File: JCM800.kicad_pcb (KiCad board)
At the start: 2 copper layers, 196 x 77.3 mm, 75 parts, among them U1 ECC83, U2 ECC83, U3 EL84

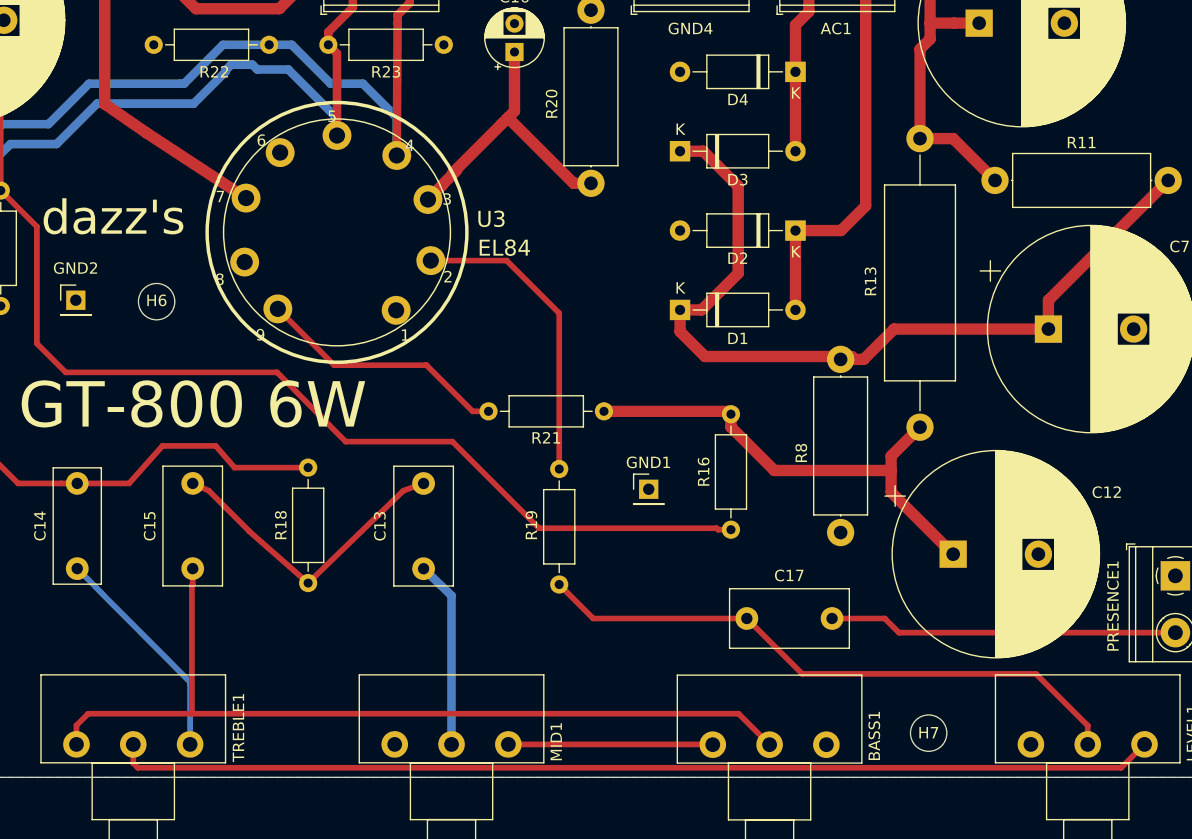
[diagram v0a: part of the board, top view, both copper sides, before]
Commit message: Added attenuation resistor
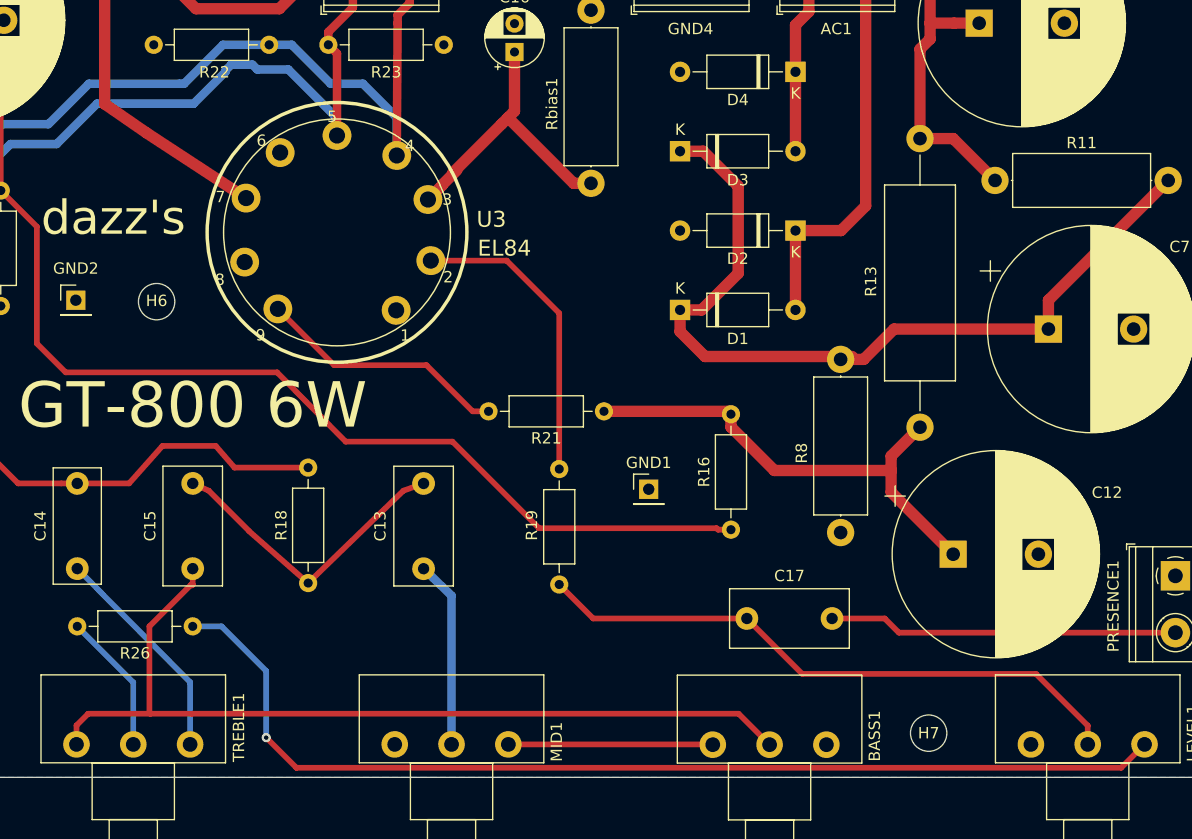
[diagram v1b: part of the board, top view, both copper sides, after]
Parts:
- added R26: ?R, Resistor_THT:R_Axial_DIN0207_L6.3mm_D2.5mm_P10.16mm_Horizontal, F.Cu at (151.1, 118.1)
- renumbered R20 to Rbias1
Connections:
- TREBLE1 pad 2: Net-(LEVEL1-Pad3) -> Net-(R26-Pad2)
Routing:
- net Net-(R26-Pad2): track 0.00 -> 12.4 mm
- net Net-(BASS1-Pad2): track 78.1 -> 79.8 mm
- net Net-(LEVEL1-Pad3): track 91.7 -> 93.2 mm, vias 0 -> 1

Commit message: Tweaks
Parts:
- C16: footprint Capacitor_THT:CP_Radial_D5.0mm_P2.50mm -> Capacitor_THT:CP_Radial_D8.0mm_P3.50mm
- moved Rbias1 0.38 mm to (186.6, 63.9)
- moved C16 0.25 mm to (179.2, 67.6)
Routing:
- net /B1: track 107.1 -> 105.9 mm

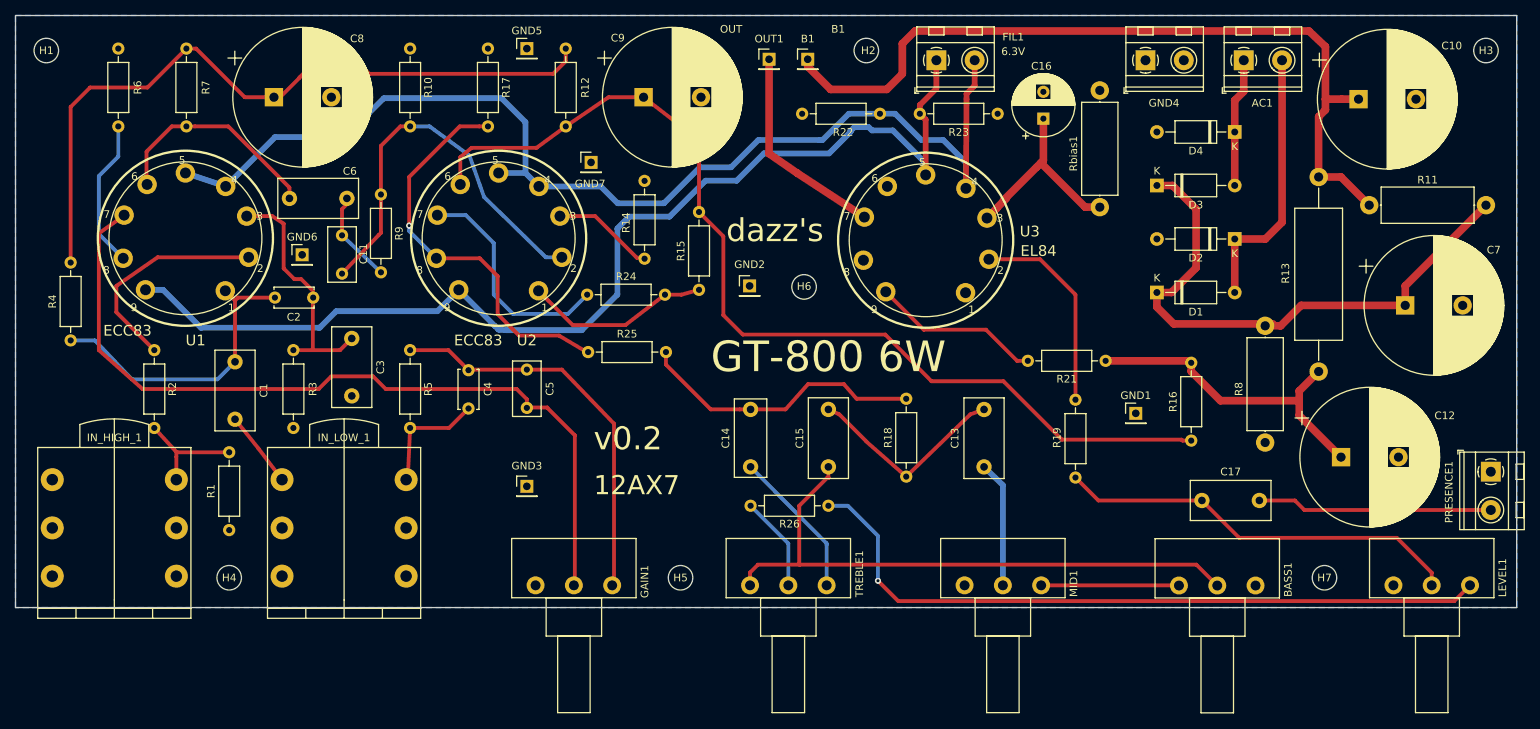
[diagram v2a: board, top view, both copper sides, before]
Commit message: Gain trace shielded
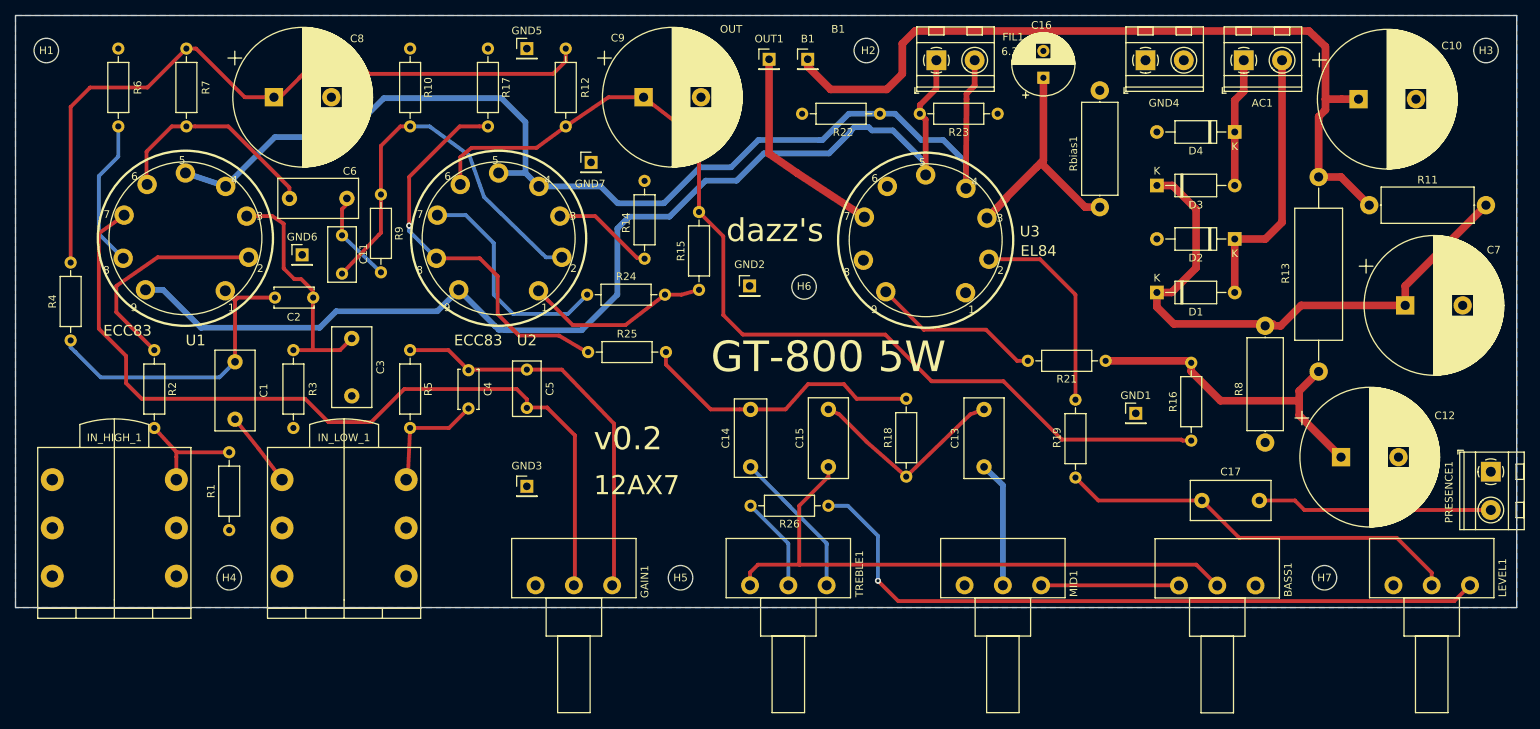
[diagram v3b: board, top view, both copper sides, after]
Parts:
- moved C16 5.33 mm to (179.2, 62.2)
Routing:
- net /EL84-CATHODE: track 26.5 -> 31.9 mm
- net Net-(C5-Pad2): track 107.6 -> 110.4 mm
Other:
- board text added: "GT-800 5W"
- board text removed: "GT-800 6W"
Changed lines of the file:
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@@
     (thickness 1.6)
     (drawings 11)
-    (tracks 325)
+    (tracks 329)
     (zones 0)
     (modules 76)
@@
     (add_net "Net-(BASS1-Pad1)")
     (add_net "Net-(BASS1-Pad2)")
+    (add_net "Net-(C1-Pad1)")
     (add_net "Net-(C1-Pad2)")
     (add_net "Net-(C11-Pad1)")
@@
     (uvia_dia 0.3)
     (uvia_drill 0.1)
-    (add_net "Net-(C1-Pad1)")
     (add_net "Net-(C13-Pad1)")
     (add_net "Net-(C14-Pad2)")
@@
   )
   (module Capacitor_THT:CP_Radial_D8.0mm_P3.50mm (layer F.Cu)
-    (at 179.197 67.564 90)
+    (at 179.197 62.23 90)
     (descr "CP, Radial series, Radial, pin pitch=3.50mm, , diameter=8mm, Electrolytic Capacitor")
     (tags "CP Radial series Radial pin pitch 3.50mm  diameter 8mm Electrolytic Capacitor")
@@
     (effects (font (size 3 3) (thickness 0.3)))
   )
-  (gr_text "GT-800 6W" (at 151.13 98.679) (layer F.SilkS)
+  (gr_text "GT-800 5W" (at 151.13 98.679) (layer F.SilkS)
     (effects (font (size 4 4) (thickness 0.5)))
   )
@@
   (segment (start 74.040998 90.932) (end 73.659999 91.312999) (width 0.5) (layer F.Cu) (net 4))
   (segment (start 78.867 90.932) (end 74.040998 90.932) (width 0.5) (layer F.Cu) (net 4) (status 10))
-  (segment (start 71.374 101.6) (end 73.66 99.314) (width 0.5) (layer B.Cu) (net 4) (status 20))
-  (segment (start 55.36037 96.52) (end 52.197 96.52) (width 0.5) (layer B.Cu) (net 4) (status 20))
-  (segment (start 60.198 101.6) (end 71.374 101.6) (width 0.5) (layer B.Cu) (net 4))
-  (segment (start 55.36037 96.52) (end 60.198 101.6) (width 0.5) (layer B.Cu) (net 4))
+  (segment (start 52.832 98.044) (end 52.180868 97.424058) (width 0.5) (layer B.Cu) (net 4))
+  (segment (start 56.134 101.346) (end 52.832 98.044) (width 0.5) (layer B.Cu) (net 4))
+  (segment (start 73.66 99.314) (end 71.628 101.346) (width 0.5) (layer B.Cu) (net 4))
+  (segment (start 71.628 101.346) (end 56.134 101.346) (width 0.5) (layer B.Cu) (net 4))
+  (segment (start 52.180868 96.536132) (end 52.197 96.52) (width 0.5) (layer B.Cu) (net 4))
+  (segment (start 52.180868 97.424058) (end 52.180868 96.536132) (width 0.5) (layer B.Cu) (net 4))
   (segment (start 83.82 97.79) (end 83.82 90.043) (width 0.5) (layer F.Cu) (net 5))
   (segment (start 83.82 90.043) (end 82.296 88.519) (width 0.5) (layer F.Cu) (net 5))
@@
   (segment (start 114.427 105.316) (end 118.03 108.919) (width 0.5) (layer F.Cu) (net 9))
   (segment (start 114.427 105.283) (end 114.427 105.316) (width 0.5) (layer F.Cu) (net 9))
-  (segment (start 111.76 104.19863) (end 111.76 105.33) (width 0.5) (layer F.Cu) (net 9) (status 20))
-  (segment (start 110.43137 102.87) (end 111.76 104.19863) (width 0.5) (layer F.Cu) (net 9))
-  (segment (start 93.345 102.87) (end 110.43137 102.87) (width 0.5) (layer F.Cu) (net 9))
-  (segment (start 91.694 101.219) (end 93.345 102.87) (width 0.5) (layer F.Cu) (net 9))
-  (segment (start 55.88 82.55) (end 55.88 97.79) (width 0.5) (layer F.Cu) (net 9))
-  (segment (start 59.25 80.166) (end 55.88 82.55) (width 0.5) (layer F.Cu) (net 9) (status 10))
-  (segment (start 55.88 97.79) (end 61.595 102.87) (width 0.5) (layer F.Cu) (net 9))
-  (segment (start 61.595 102.87) (end 84.582 102.87) (width 0.5) (layer F.Cu) (net 9))
-  (segment (start 84.582 102.87) (end 86.233 101.219) (width 0.5) (layer F.Cu) (net 9))
-  (segment (start 86.233 101.219) (end 91.694 101.219) (width 0.5) (layer F.Cu) (net 9))
+  (segment (start 55.88 82.55) (end 59.25 80.166) (width 0.5) (layer F.Cu) (net 9))
+  (segment (start 55.88 94.996) (end 55.88 82.55) (width 0.5) (layer F.Cu) (net 9))
+  (segment (start 59.436 98.552) (end 55.88 94.996) (width 0.5) (layer F.Cu) (net 9))
+  (segment (start 59.436 102.108) (end 59.436 98.552) (width 0.5) (layer F.Cu) (net 9))
+  (segment (start 61.468 104.14) (end 59.436 102.108) (width 0.5) (layer F.Cu) (net 9))
+  (segment (start 82.804 104.14) (end 61.468 104.14) (width 0.5) (layer F.Cu) (net 9))
+  (segment (start 111.76 104.19863) (end 110.43137 102.87) (width 0.5) (layer F.Cu) (net 9))
+  (segment (start 111.76 105.33) (end 111.76 104.19863) (width 0.5) (layer F.Cu) (net 9))
+  (segment (start 110.43137 102.87) (end 95.758 102.87) (width 0.5) (layer F.Cu) (net 9))
+  (segment (start 95.758 102.87) (end 91.44 107.188) (width 0.5) (layer F.Cu) (net 9))
+  (segment (start 91.44 107.188) (end 85.852 107.188) (width 0.5) (layer F.Cu) (net 9))
+  (segment (start 85.852 107.188) (end 82.804 104.14) (width 0.5) (layer F.Cu) (net 9))
   (segment (start 87.63 79.375) (end 87.63 82.55) (width 0.5) (layer F.Cu) (net 10) (status 20))
   (segment (start 87.63 79.375) (end 89.027 77.978) (width 0.5) (layer F.Cu) (net 10) (status 20))
@@
   (segment (start 178.308 73.914) (end 173.99 78.232) (width 1) (layer F.Cu) (net 37))
   (segment (start 178.308 73.914) (end 178.8795 73.3425) (width 1) (layer F.Cu) (net 37))
-  (segment (start 179.197 73.025) (end 178.8795 73.3425) (width 1) (layer F.Cu) (net 37))
-  (segment (start 179.197 67.564) (end 179.197 73.025) (width 1) (layer F.Cu) (net 37))
   (segment (start 184.658 79.121) (end 186.563 79.121) (width 1) (layer F.Cu) (net 37))
   (segment (start 178.8795 73.3425) (end 184.658 79.121) (width 1) (layer F.Cu) (net 37))
+  (segment (start 179.197 73.025) (end 178.8795 73.3425) (width 1) (layer F.Cu) (net 37))
+  (segment (start 179.197 62.23) (end 179.197 73.025) (width 1) (layer F.Cu) (net 37))
   (segment (start 96.393 75.184) (end 102.997 68.58) (width 0.5) (layer F.Cu) (net 38))
   (segment (start 102.997 68.58) (end 105.54863 68.58) (width 0.5) (layer F.Cu) (net 38))
@@
   )
   (zone (net 0) (net_name "") (layer B.Cu) (hatch edge 0.508)
-    (connect_pads (clearance 0.508))
+    (connect_pads (clearance 1))
     (min_thickness 0.254)
-    (keepout (tracks not_allowed) (vias not_allowed) (copperpour not_allowed))
+    (keepout (tracks allowed) (vias allowed) (copperpour not_allowed))
     (fill (arc_segments 32) (thermal_gap 0.508) (thermal_bridge_width 0.508))
     (polygon
       (pts
-        (xy 103.6955 96.52) (xy 121.6025 96.52) (xy 128.524 103.886) (xy 139.7 114.427) (xy 139.66825 131.064)
-        (xy 116.1415 131.064) (xy 116.205 111.76) (xy 109.474 105.414995) (xy 92.57079 105.405005) (xy 91.186 102.235)
-        (xy 86.614 102.235) (xy 85.471 105.425875) (xy 60.70104 105.403055) (xy 58.170961 102.114945) (xy 73.466524 102.107008)
-        (xy 75.123477 99.822992) (xy 93.6625 99.822) (xy 95.25 97.79) (xy 102.87 97.79)
+        (xy 126.873 131.064) (xy 126.873 107.188) (xy 117.094 97.409) (xy 105.664 97.409) (xy 102.362 97.409)
+        (xy 89.535 97.409) (xy 87.122 94.996) (xy 71.628 94.996) (xy 71.628 98.552) (xy 85.09 98.552)
+        (xy 87.376 100.838) (xy 115.062 100.838) (xy 123.444 109.22) (xy 123.444 131.064)
       )
     )

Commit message: Added Johnston's toad logo
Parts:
- added G***: LOGO, toad-logo:toad-big, F.Cu at (126.7, 111.5)

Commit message: Logo
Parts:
- moved G*** 1.27 mm to (126.7, 110.2)
- moved GND2 0.28 mm to (141.0, 89.7)
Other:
- board text added: "dazz"
- board text removed: "dazz's"
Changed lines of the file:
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@@
   )
   (module toad-logo:toad-big (layer F.Cu)
-    (at 126.746 111.506)
+    (at 126.746 110.236)
     (fp_text reference G*** (at 0 0) (layer F.SilkS) hide
       (effects (font (size 1.524 1.524) (thickness 0.3)))
@@
   )
   (module Connector_PinHeader_2.54mm:PinHeader_1x01_P2.54mm_Vertical (layer F.Cu)
-    (at 140.843 89.408)
+    (at 140.97 89.662)
     (descr "Through hole straight pin header, 1x01, 2.54mm pitch, single row")
     (tags "Through hole pin header THT 1x01 2.54mm single row")
@@
     )
   )
-  (gr_text dazz's (at 144.272 76.2) (layer F.SilkS)
-    (effects (font (size 3 3) (thickness 0.5)))
+  (gr_text dazz (at 118.11 119.126) (layer F.SilkS)
+    (effects (font (size 1.5 1.5) (thickness 0.3)))
   )
   (gr_text 6.3V (at 175.26 58.801) (layer F.SilkS)
     (effects (font (size 1 1) (thickness 0.15)))
   )
-  (gr_text 12AX7 (at 183.515 92.329) (layer F.SilkS)
+  (gr_text 12AX7 (at 183.388 90.678) (layer F.SilkS)
     (effects (font (size 2.5 2.5) (thickness 0.3)))
   )
@@
     (effects (font (size 1 1) (thickness 0.15)))
   )
-  (gr_text v0.2 (at 182.372 86.233) (layer F.SilkS)
+  (gr_text v0.2 (at 144.272 80.772) (layer F.SilkS)
     (effects (font (size 3 3) (thickness 0.3)))
   )
